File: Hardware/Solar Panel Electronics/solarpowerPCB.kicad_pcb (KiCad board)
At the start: 4 copper layers, 57.8 x 69.2 mm, 157 parts, among them J1 Screw_Terminal_SolarPanel_Inp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, J10 Screw_Terminal_SolarPanel_Inp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, J11 Screw_Terminal_SolarPanel_Inp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, J12 NTC Connector, J13 Battery Connector, J14 Screw_Terminal_5VRail, J2 Screw_Terminal_SolarPanel_Inp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, J3 Conn_01x02_Male, J4 Conn_01x06_Male, J5 Conn_01x02_Male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

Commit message: routing clean up
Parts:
- moved C33 5.10 mm to (73.2, 115.8)
- moved R4 4.40 mm to (71.1, 113.5)
- moved R16 4.35 mm to (75.4, 113.5)
- moved Q1 4.35 mm to (73.2, 113.4)
- moved R48 1.90 mm to (75.5, 110.2), turned to -90 degrees
- moved R44 1.42 mm to (70.9, 116.5)
- moved C34 1.42 mm to (69.4, 116.5)
- moved R45 1.38 mm to (67.9, 116.5)
- moved C10 1.20 mm to (63.9, 122.8)
- moved C35 1.20 mm to (64.6, 125.2)
- moved C8 1.20 mm to (65.4, 122.8)
- moved R46 0.53 mm to (65.9, 118.8)
- moved R40 0.47 mm to (72.8, 124.3)
- moved R20 0.45 mm to (56.5, 117.2)
- moved TP2 0.43 mm to (61.9, 112.0)
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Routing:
- net /SolarPanelVoltage2: track 1.50 -> 55.4 mm, vias 0 -> 2
- net /~{SD_CS}: track 2.78 -> 48.6 mm, vias 1 -> 3
- net /SolarPanelVoltage1: track 1.50 -> 46.8 mm, vias 0 -> 4
- net /HSPI_MISO: track 0.00 -> 34.5 mm, vias 0 -> 1
- net /CLKOUT: track 3.19 -> 35.6 mm, vias 1 -> 2
- net /HSPI_MOSI: track 0.00 -> 30.9 mm, vias 0 -> 1
- net /HSPI_SCLK: track 0.00 -> 30.2 mm, vias 0 -> 1
- net /VSPI_MISO: track 11.8 -> 36.8 mm, vias 1 -> 4
- net /VSPI_SCLK: track 11.0 -> 35.7 mm, vias 1 -> 4
- net /SDA: track 48.0 -> 64.3 mm
- net /EN: track 56.9 -> 67.0 mm
- net /SCL: track 47.6 -> 55.9 mm
- net /VoltageReg/V_reg: track 77.5 -> 70.9 mm
- net /DTR: track 37.7 -> 42.8 mm
- net /ADC/AIN3P: track 29.7 -> 26.0 mm
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
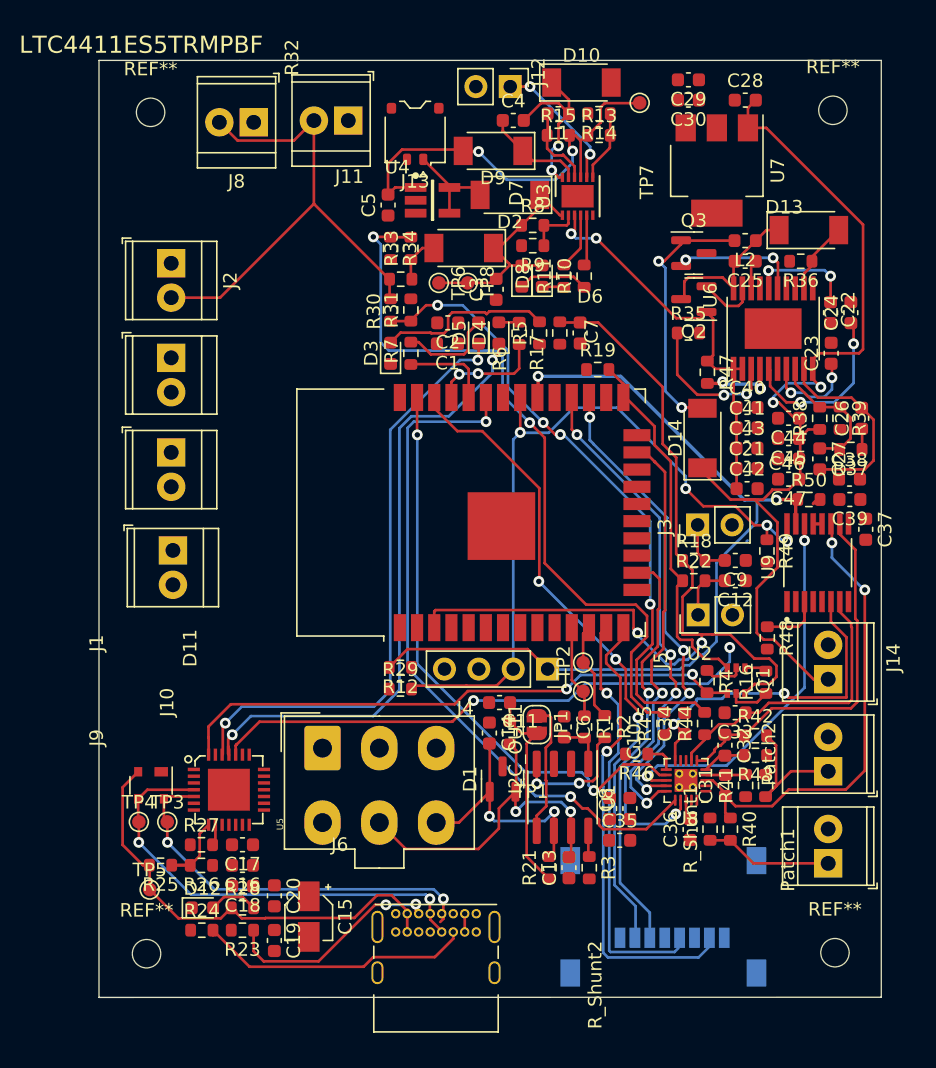
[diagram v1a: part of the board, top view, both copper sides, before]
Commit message: Almost finished routing
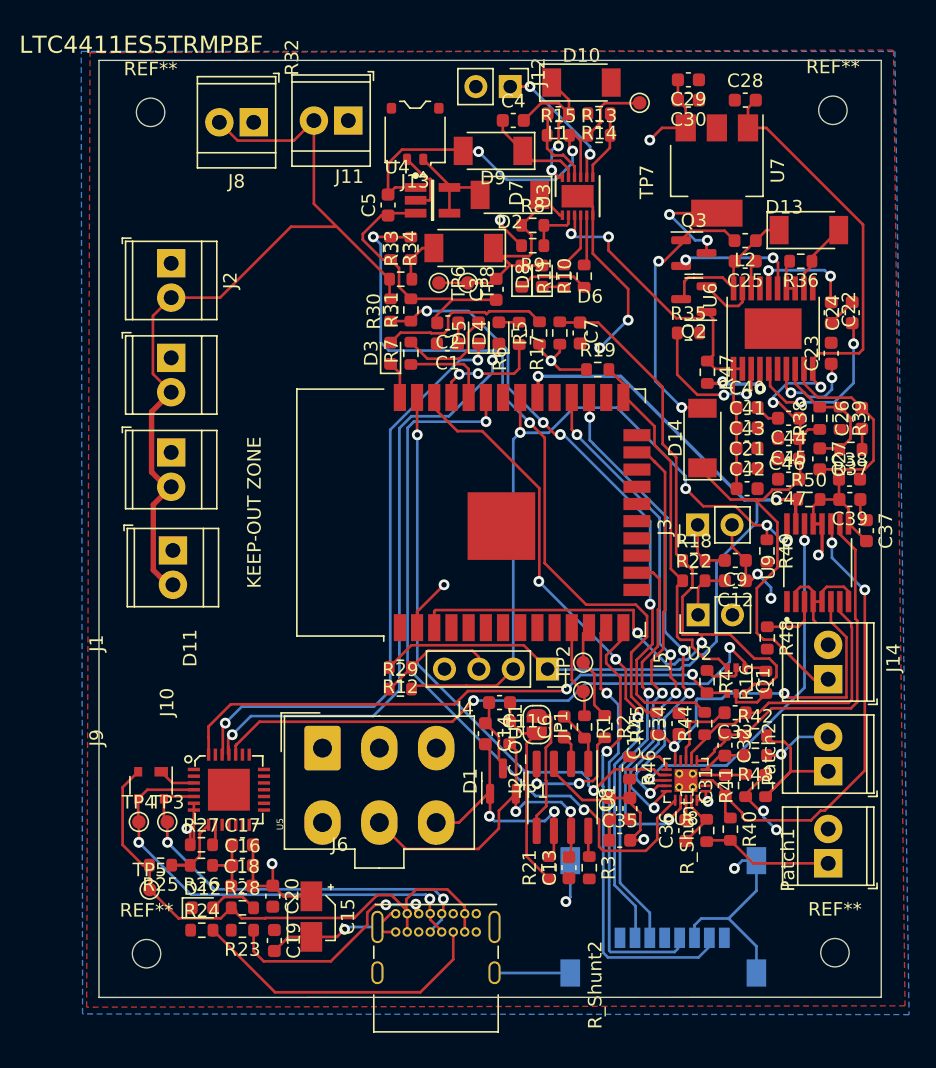
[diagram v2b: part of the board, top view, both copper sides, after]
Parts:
- moved R46 1.15 mm to (65.3, 119.8), turned to -90 degrees
- moved R45 0.55 mm to (67.3, 116.5)
- moved C34 0.42 mm to (69.0, 116.5)
- moved C36 0.33 mm to (69.5, 124.5)
- moved C14 0.30 mm to (54.7, 117.3)
- moved R_Shunt1 0.27 mm to (71.0, 124.5)
- moved C15 0.19 mm to (41.9, 130.8)
- moved D1 0.15 mm to (56.0, 120.8)
- moved C20 0.12 mm to (39.0, 129.3)
- moved C37 0.11 mm to (82.8, 102.3)
- moved C24 0.10 mm to (81.8, 86.2)
- moved C18 0.07 mm to (36.7, 128.6), turned to 0 degrees
- turned C16 to 0 degrees
- turned C17 to 0 degrees
- turned C6 to 90 degrees
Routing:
- net GND: track 0.00 -> 150.7 mm, vias 0 -> 13
- net +3V3: track 1.47 -> 68.3 mm, vias 0 -> 8
- net /Solar Charger/V_solarpanel: track 37.1 -> 63.8 mm
- net VBUS: track 35.3 -> 41.8 mm
- net /VSolCharger: track 47.8 -> 51.6 mm
- net /VSPI_MOSI: track 51.3 -> 54.6 mm
- net Net-(J6-PadB5): track 20.6 -> 23.1 mm
- net /ADC/AIN3P: track 26.0 -> 28.3 mm
- net /RTS: track 42.5 -> 44.5 mm
- net Net-(Patch2-Pad1): track 10.5 -> 11.9 mm
- net /ADC/AIN0P: track 34.8 -> 35.9 mm
- net Net-(R46-Pad1): track 2.36 -> 3.36 mm
- net Net-(D14-Pad2): track 19.5 -> 20.3 mm
- net Net-(C6-Pad2): track 4.08 -> 4.85 mm
- net /usb_to_uart/Data-: track 31.3 -> 30.6 mm
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- added copper zone on B.Cu, net +3V3
- added copper zone on F.Cu, net GND

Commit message: PCB done. Just needs checking
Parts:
- moved C33 1.41 mm to (74.5, 116.1)
- moved C25 1.09 mm to (72.8, 82.4)
- moved L2 1.09 mm to (72.8, 80.9)
- moved R24 0.93 mm to (34.5, 132.4), turned to -90 degrees
- moved Q3 0.75 mm to (69.3, 81.8)
- moved D12 0.70 mm to (33.7, 129.5)
- moved R39 0.50 mm to (81.4, 94.0), turned to 90 degrees
- moved R40 0.46 mm to (72.3, 124.4)
- moved R35 0.42 mm to (69.6, 88.1), turned to 180 degrees
- moved C26 0.40 mm to (82.9, 94.0)
- moved TP1 0.40 mm to (62.3, 114.0)
- moved J4 0.36 mm to (42.4, 118.5)
- moved TP2 0.36 mm to (62.3, 112.0)
- moved R_Shunt2 0.36 mm to (75.5, 121.5)
- moved R41 0.35 mm to (74.0, 121.5)
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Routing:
- net GND: track 150.7 -> 273.1 mm, vias 13 -> 30
- net +3V3: track 68.3 -> 107.9 mm, vias 8 -> 15
- net VBUS: track 41.8 -> 48.8 mm
- net /VSolCharger: track 51.6 -> 58.5 mm, vias 2 -> 4
- net /VSPI_MOSI: track 54.6 -> 59.4 mm
- net Net-(D3-Pad2): track 13.0 -> 16.2 mm
- net /Solar Charger/V_solarpanel: track 63.8 -> 67.0 mm
- net Net-(Patch2-Pad1): track 11.9 -> 9.45 mm
- net /SCL: track 55.9 -> 58.2 mm
- net /ADC/~{DRDY}: track 27.6 -> 29.6 mm
- net Net-(J6-PadA5): track 16.9 -> 18.7 mm
- net Net-(C26-Pad2): track 14.6 -> 16.3 mm
- net Net-(C25-Pad2): track 11.8 -> 13.5 mm
- net Net-(Q3-Pad2): track 9.53 -> 11.2 mm
- net Net-(R35-Pad1): track 10.9 -> 9.40 mm
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
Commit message: ICARUS v2
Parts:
- removed C35, C37: 10uF, Capacitor_SMD:C_0603_1608Metric
- removed C36: 220nF, Capacitor_SMD:C_0603_1608Metric
- removed J10, J11, J2, J8, J9: Screw_Terminal_SolarPanel_Input, TerminalBlock_TE-Connectivity:TerminalBlock_TE_282834-2_1x02_P2.54mm_Horizontal
- removed J12: NTC Connector, Connector_PinHeader_2.54mm:PinHeader_1x02_P2.54mm_Vertical
- removed J14: Screw_Terminal_5VRail, TerminalBlock_TE-Connectivity:TerminalBlock_TE_282834-2_1x02_P2.54mm_Horizontal
- removed R46: 10k, Resistor_SMD:R_0603_1608Metric
- removed the REF** at (29.7, 133.6)
- removed the REF** at (80.5, 133.5)
- removed the REF** at (80.4, 71.2)
- removed the REF** at (30.0, 71.4)
- removed TP1, TP2: TestPoint, TestPoint:TestPoint_Pad_D1.0mm
- removed U8: ADS131M04, Package_DFN_QFN:WQFN-20-1EP_3x3mm_P0.4mm_EP1.7x1.7mm_ThermalVias
- added G***: LOGO, iclr:iclr_logo, B.Cu at (129.0, 92.2)
- added G***: LOGO, iclr:icarus2.0, B.Cu at (149.4, 113.7)
- added REF**: MountingHole_3.2mm_M3_DIN965_Pad, MountingHole:MountingHole_3.2mm_M3_DIN965_Pad, F.Cu at (125.4, 83.9)
- added REF**: MountingHole_3.2mm_M3_DIN965_Pad, MountingHole:MountingHole_3.2mm_M3_DIN965_Pad, F.Cu at (125.4, 136.9)
- added REF**: MountingHole_3.2mm_M3_DIN965_Pad, MountingHole:MountingHole_3.2mm_M3_DIN965_Pad, F.Cu at (178.4, 136.9)
- added REF**: MountingHole_3.2mm_M3_DIN965_Pad, MountingHole:MountingHole_3.2mm_M3_DIN965_Pad, F.Cu at (178.4, 83.9)
- moved C19 138.3 mm to (177.2, 127.1), turned to 0 degrees
- moved C20 138.2 mm to (177.2, 125.6), turned to 0 degrees
- moved J13 134.5 mm to (179.3, 108.5), turned to 0 degrees
- moved C5 130.4 mm to (176.5, 97.2)
- moved J4 130.0 mm to (172.0, 128.2), turned to -90 degrees
- moved U4 127.5 mm to (176.2, 101.2), turned to -90 degrees
- moved D2 125.6 mm to (179.7, 102.3), turned to -90 degrees
- moved J1 122.0 mm to (153.4, 84.2), turned to 0 degrees
- moved D9 120.8 mm to (174.2, 95.5), turned to -90 degrees
- moved D10 119.3 mm to (178.8, 92.8), turned to -90 degrees
- moved R15 118.3 mm to (176.5, 94.1), turned to -90 degrees
- moved L1 118.1 mm to (176.5, 91.2), turned to -90 degrees
- moved C30 118.0 mm to (174.9, 124.1)
- moved TP8 117.6 mm to (169.8, 100.7), turned to 180 degrees
- moved C4 116.9 mm to (172.0, 92.7), turned to 90 degrees
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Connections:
- C33 pad 2: GND -> GNDA
- C34 pad 2: GND -> GNDA
- J1 pad 1: GND -> GNDA
- Patch1 pad 2: GND -> GNDA
- Patch2 pad 2: GND -> GNDA
- R41 pad 1: GND -> GNDA
- R43 pad 1: GND -> GNDA
- R_Shunt1 pad 2: GND -> GNDA
- R_Shunt2 pad 2: GND -> GNDA
- U2 pad 23: /CLKOUT -> unconnected-(U2-Pad23)
- U2 pad 27: /VSPI_SCLK -> unconnected-(U2-Pad27)
- U2 pad 28: /VSPI_MISO -> unconnected-(U2-Pad28)
- U2 pad 33: /VSPI_MOSI -> unconnected-(U2-Pad33)
- U2 pad 37: /~{ADC_CS} -> unconnected-(U2-Pad37)
- U3 pad 8: Net-(J12-Pad1) -> unconnected-(U3-Pad8)
- U6 pad 21: unconnected-(U6-Pad21) -> GND
- U9 pad 5: GND -> GNDA
- U9 pad 8: GND -> GNDA
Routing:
- net GND: track 273.1 -> 59.9 mm, vias 30 -> 62
- net /Solar Charger/V_solarpanel: track 67.0 -> 6.06 mm
- net /VSPI_MOSI: track 59.4 -> 0.00 mm, vias 2 -> 0
- net /SolarPanelVoltage2: track 55.1 -> 4.84 mm, vias 2 -> 0
- net /~{ADC_CS}: track 43.1 -> 0.00 mm, vias 2 -> 0
- net /SDA: track 64.5 -> 22.0 mm, vias 2 -> 0
- net /SolarPanelVoltage1: track 47.1 -> 6.12 mm, vias 4 -> 0
- net /EN: track 67.3 -> 26.4 mm
- net +3V3: track 107.9 -> 67.7 mm, vias 15 -> 13
- net /VoltageReg/V_reg: track 72.3 -> 34.1 mm, vias 2 -> 0
- net /VSPI_MISO: track 37.8 -> 0.00 mm, vias 4 -> 0
- net /RXD: track 45.5 -> 8.32 mm
- net /VSPI_SCLK: track 36.5 -> 0.00 mm, vias 4 -> 0
- net /CLKOUT: track 36.0 -> 0.00 mm, vias 2 -> 0
- net /SCL: track 58.2 -> 25.0 mm, vias 4 -> 0
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- added copper zone on B.Cu, net GND
- added copper zone on F.Cu, net GNDA
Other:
- board size 57.8 x 69.2 mm -> 60 x 60 mm
- copper layers 4 -> 2
- board text added: "Designed By: Gabisanth Seyon Danielle Bella Artem Sheykin"
- board text added: "I - Imperial C - College A - Avionics R - Run U - Using S - Solar power"
- board text added: "ICARUS v2.0"

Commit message: removed can resistors
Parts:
- removed the G*** at (129.0, 92.2)
- removed R1, R2: 90, Resistor_SMD:R_0603_1608Metric
- removed REF** (x4): MountingHole_3.2mm_M3_DIN965_Pad, MountingHole:MountingHole_3.2mm_M3_DIN965_Pad
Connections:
- C6 pad 2: Net-(C6-Pad2) -> /CAN_TX
- U1 pad 1: Net-(C6-Pad2) -> /CAN_TX
- U1 pad 4: Net-(R2-Pad2) -> /CAN_RX
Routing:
- net /CAN_TX: track 18.6 -> 23.6 mm
- net Net-(C6-Pad2): track 4.90 -> 0.00 mm
- net /CAN_RX: track 15.5 -> 19.5 mm, vias 0 -> 2
- net Net-(R2-Pad2): track 2.41 -> 0.00 mm
- net Net-(C25-Pad2): track 15.9 -> 14.7 mm

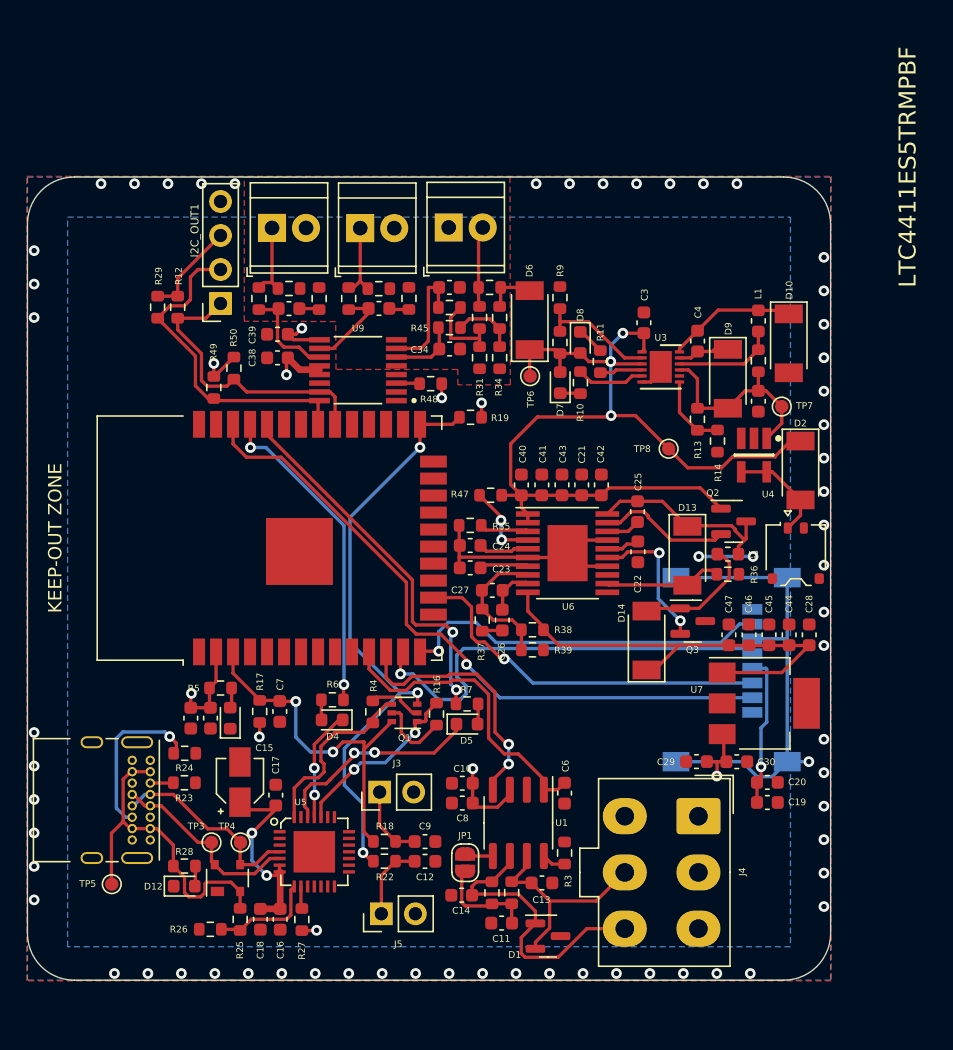
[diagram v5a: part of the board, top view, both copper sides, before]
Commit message: removed ltc4411 on solar charger, added solder jumpers
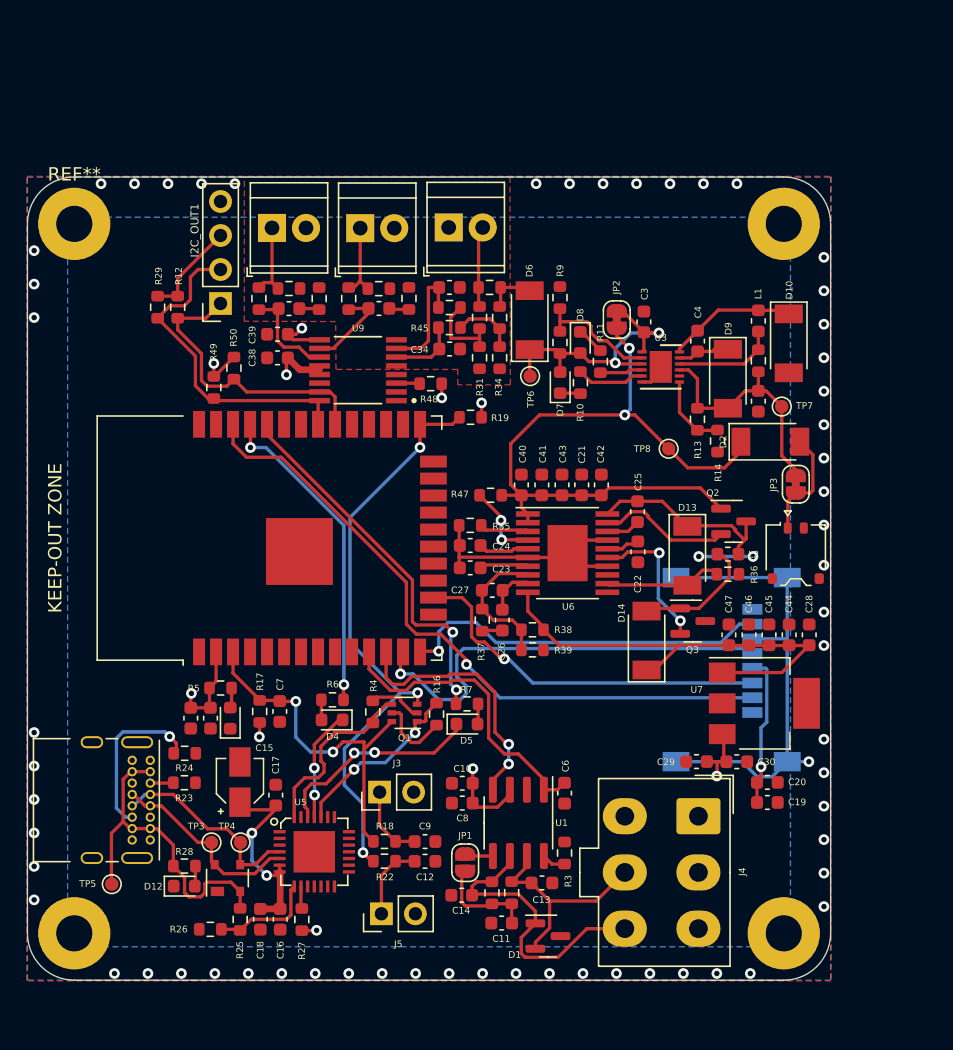
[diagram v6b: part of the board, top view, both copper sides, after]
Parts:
- removed U4: LTC4411ES5TRMPBF, LTC4411:Linear_Technology-LTC4411ES5TRMPBF-Level_A
- added ?: , , F.Cu at (178.4, 136.9)
- added ?: , , F.Cu at (125.4, 136.9)
- added ?: , , F.Cu at (178.4, 83.9)
- added G***: LOGO, iclr:iclr_logo, B.Cu at (129.2, 92.4)
- added JP2: SolderJumper_2_Bridged, Jumper:SolderJumper-2_P1.3mm_Bridged_RoundedPad1.0x1.5mm, F.Cu at (165.9, 91.0)
- added JP3: SolderJumper_2_Bridged, Jumper:SolderJumper-2_P1.3mm_Bridged_RoundedPad1.0x1.5mm, F.Cu at (179.3, 103.3)
- added REF**: MountingHole_2.7mm_Pad, MountingHole:MountingHole_2.7mm_Pad, F.Cu at (125.4, 83.9)
- moved D2 3.11 mm to (177.4, 100.2), turned to 0 degrees
- moved C3 0.07 mm to (167.9, 91.2)
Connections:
- C3 pad 2: /VSolCharger -> Net-(D6-Pad1)
- D6 pad 1: /VSolCharger -> Net-(D6-Pad1)
- D7 pad 2: /VSolCharger -> Net-(D6-Pad1)
- D8 pad 2: /VSolCharger -> Net-(D6-Pad1)
- R8 pad 1: /VSolCharger -> Net-(D6-Pad1)
- TP6 pad 1: /VSolCharger -> Net-(D6-Pad1)
- U3 pad 1: /VSolCharger -> Net-(D6-Pad1)
- U3 pad 3: /VSolCharger -> Net-(D6-Pad1)
- U6 pad 21: GND -> unconnected-(U6-Pad21)
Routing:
- net Net-(D6-Pad1): track 0.00 -> 22.5 mm, vias 0 -> 2
- net /VSolCharger: track 70.5 -> 51.7 mm, vias 3 -> 2
- net Net-(C5-Pad2): track 15.4 -> 18.1 mm

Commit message: final?
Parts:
- C1: value C_Small -> 10uF
- C15: value 4.7uF -> 47uF; footprint Capacitor_SMD:CP_Elec_3x5.3 -> Capacitor_SMD:C_0603_1608Metric
- C2: value C_Small -> 0.1uF
- C7: value 0.1uF -> 1uF
- L1, L2: footprint Inductor_SMD:L_0603_1608Metric -> Inductor_SMD:L_0805_2012Metric
- R38: value 900 -> 1000
- R39: value 300 -> 332
- R5, R6, R7: value R_Small -> 470
- moved C15 1.54 mm to (139.0, 126.6), turned to -90 degrees
- moved D10 0.46 mm to (179.2, 92.8)
- moved L1 0.32 mm to (176.6, 90.8)
- moved L2 0.30 mm to (174.5, 108.7)
- moved R36 0.27 mm to (174.2, 110.3)
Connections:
- ? pad 1: (no net) -> GND (x3)
- C15 pad 1: +3V3 -> GND
- C15 pad 2: GND -> +3V3
- REF** pad 1: (no net) -> GND
- U5 pad 29: unconnected-(U5-Pad29) -> GND
- U6 pad 21: unconnected-(U6-Pad21) -> GND
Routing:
- net GND: track 59.9 -> 65.5 mm
- net +3V3: track 67.7 -> 66.2 mm
- net Net-(C4-Pad2): track 9.71 -> 10.6 mm

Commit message: Moved net from GPIO12
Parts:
- removed ? (x3): , 
- removed the G*** at (129.2, 92.4)
- removed REF**: MountingHole_2.7mm_Pad, MountingHole:MountingHole_2.7mm_Pad
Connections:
- U2 pad 10: unconnected-(U2-Pad10) -> /HSPI_MISO
- U2 pad 14: /HSPI_MISO -> unconnected-(U2-Pad14)
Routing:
- net /HSPI_MISO: track 27.8 -> 35.1 mm
